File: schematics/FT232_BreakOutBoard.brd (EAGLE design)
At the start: 44.1 x 21.6 mm, 13 parts, among them IC2 FT232RL

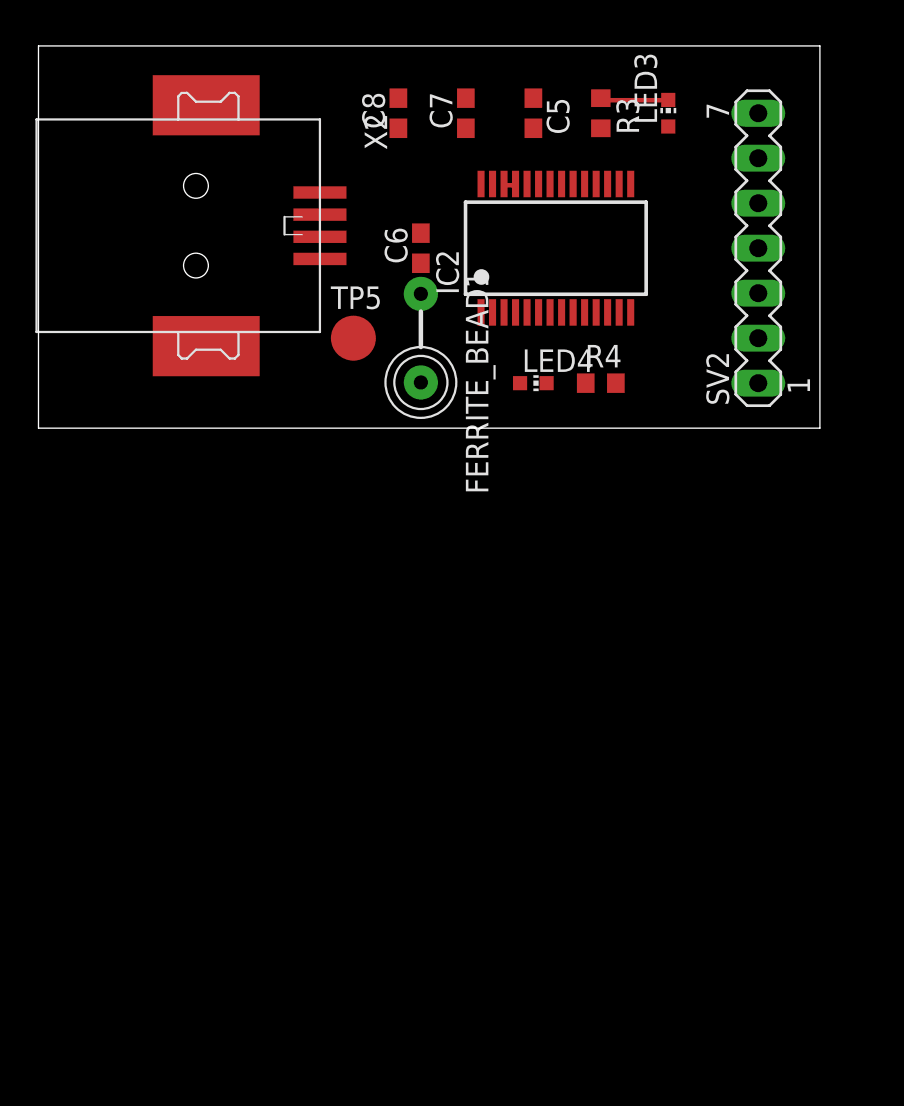
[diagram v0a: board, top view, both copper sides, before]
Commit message: updated breakout board layout and schematic
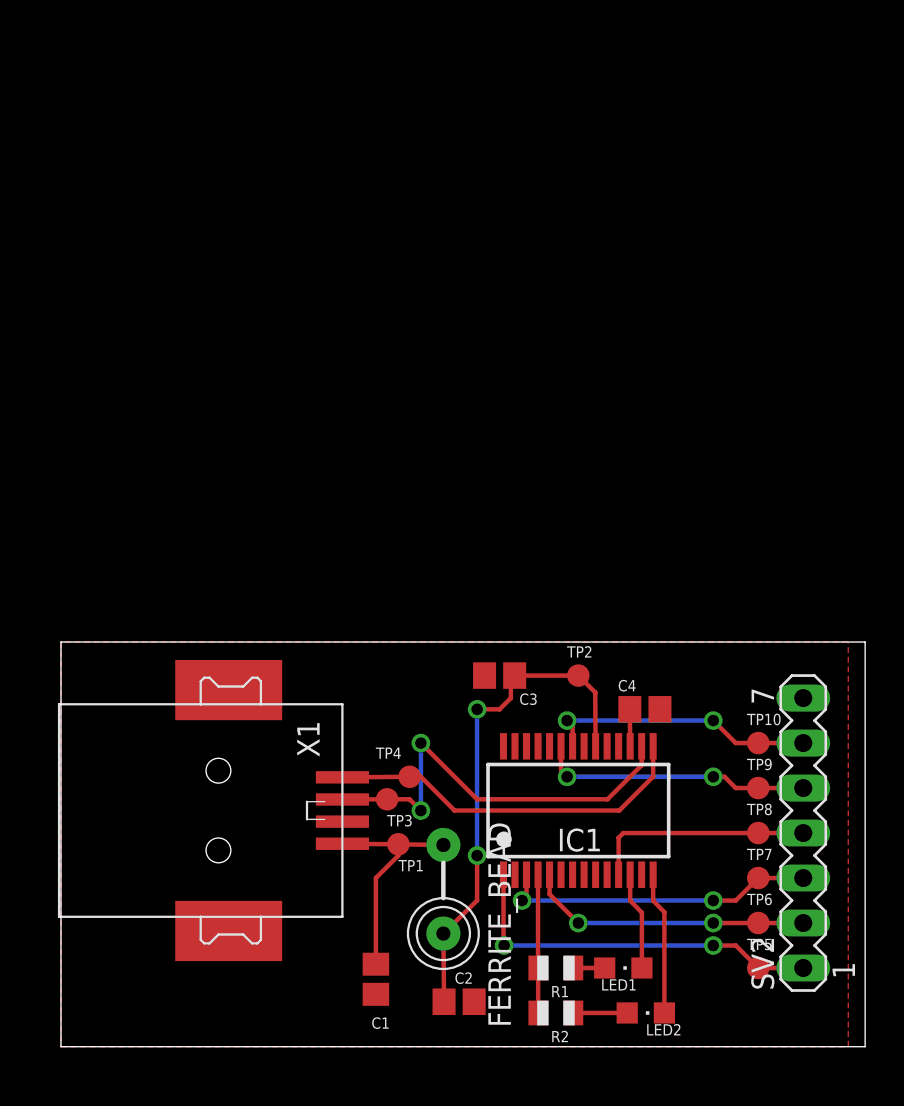
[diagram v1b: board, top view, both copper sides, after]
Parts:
- removed C5, C7: 0.1uF, adafruit:C0603
- removed C6: 10nF, adafruit:C0603
- removed C8: 10uF, adafruit:C0603
- removed FERRITE_BEAD1: FB, adafruit:FB
- removed IC2: FT232RL, ftdichip:SSOP28
- removed LED3, LED4: (no value), adafruit:CHIP-LED0603
- removed R3, R4: 1k, adafruit:R0603
- removed X2: (no value), con-usb-3:USB-B-SMT
- added C1: 10nF, adafruit:C0805
- added C2, C4: 100nF, adafruit:C0805
- added C3: 4.7uF, adafruit:C0805
- added FERRITE_BEAD: FB, adafruit:FB
- added IC1: FT232RL, ftdichip:SSOP28
- added LED1, LED2: (no value), adafruit:CHIPLED_0805
- added R1, R2: (no value), adafruit:R0805
- added TP1, TP10, TP2, TP3, TP4, TP6, TP7, TP8, TP9: TPB1,27, testpad:B1,27
- added X1: USB-B-S, con-usb:USB-B-SMT
- TP5: value TPB2,54 -> TPB1,27; device testpad:B2,54 -> testpad:B1,27
- moved TP5 42.3 mm to (40.6, -19.1)
- moved SV2 33.1 mm to (43.2, -11.4)
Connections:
- removed net N$19: IC2.22, R3.2
- removed net N$20: LED3.C, R3.1
- removed net N$21: C7.1, C8.1, FERRITE_BEAD1.P$2, IC2.20, IC2.4, LED3.A, LED4.A
- removed net N$22: C5.1, IC2.17
- removed net N$23: IC2.15, X2.D+
- removed net N$24: IC2.16, X2.D-
- removed net N$25: IC2.13, R4.2
- removed net N$26: IC2.1, SV2.1
- removed net N$27: LED4.C, R4.1
- removed net N$28: IC2.5, SV2.3
- removed net N$29: IC2.3, SV2.2
- removed net N$31: IC2.23, SV2.7
- removed net N$36: C6.1, FERRITE_BEAD1.P$1, TP5.TP, X2.VUSB
- new net DELEETE: IC1.4, R1.2, R2.2
- new net N$10: IC1.11, SV2.4, TP8.TP
- new net N$11: IC1.23, SV2.5, TP9.TP
- new net N$12: LED2.A, R2.1
- new net N$13: LED1.A, R1.1
- new net N$14: IC1.22, SV2.6, TP10.TP
- new net N$15: IC1.12, LED1.C
- new net N$16: IC1.14, LED2.C
- new net N$17: C2.1, C3.1, FERRITE_BEAD.P$2, IC1.20, TP2.TP
- new net N$6: IC1.1, SV2.1, TP5.TP
- new net N$7: C1.1, FERRITE_BEAD.P$1, TP1.TP, X1.VUSB
- new net N$8: IC1.5, SV2.2, TP6.TP
- new net N$9: IC1.3, SV2.3, TP7.TP
- net GND: now also C1.2, C2.2, C3.2, C4.2, IC1.18, IC1.21, IC1.25, IC1.7; no longer C5.2, C6.2, C7.2, C8.2, IC2.18, IC2.21, IC2.25, IC2.26, IC2.7, X2.GND
- net N$2: now also C4.1, IC1.17; no longer IC2.12, SV2.4
- net N$3: now also IC1.15, TP4.TP, X1.D+; no longer IC2.19, SV2.6
- net N$5: now also IC1.16, TP3.TP, X1.D-; no longer IC2.11, SV2.5
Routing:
- net N$17: track 0.00 -> 28.8 mm, vias 0 -> 2
- net N$5: track 0.00 -> 24.1 mm, vias 0 -> 2
- net N$6: track 0.00 -> 21.4 mm, vias 0 -> 2
- net N$3: track 0.00 -> 20.8 mm
- net N$9: track 0.00 -> 18.0 mm, vias 0 -> 2
- net N$8: track 0.00 -> 16.1 mm, vias 0 -> 2
- net N$11: track 0.00 -> 15.5 mm, vias 0 -> 2
- net N$14: track 0.00 -> 15.4 mm, vias 0 -> 2
- net N$7: track 0.00 -> 14.3 mm
- net N$10: track 0.00 -> 12.6 mm
- net N$16: track 0.00 -> 8.07 mm
- net DELEETE: track 0.00 -> 7.81 mm
- net N$15: track 0.00 -> 5.54 mm
- net N$20: track 3.90 -> 0.00 mm
- net N$12: track 0.00 -> 3.03 mm
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- added copper zone on layer 1, net GND
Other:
- board size 44.1 x 21.6 mm -> 45.4 x 22.9 mm

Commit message: Updated FT232 break-out board with corrected USB connector and larger vias
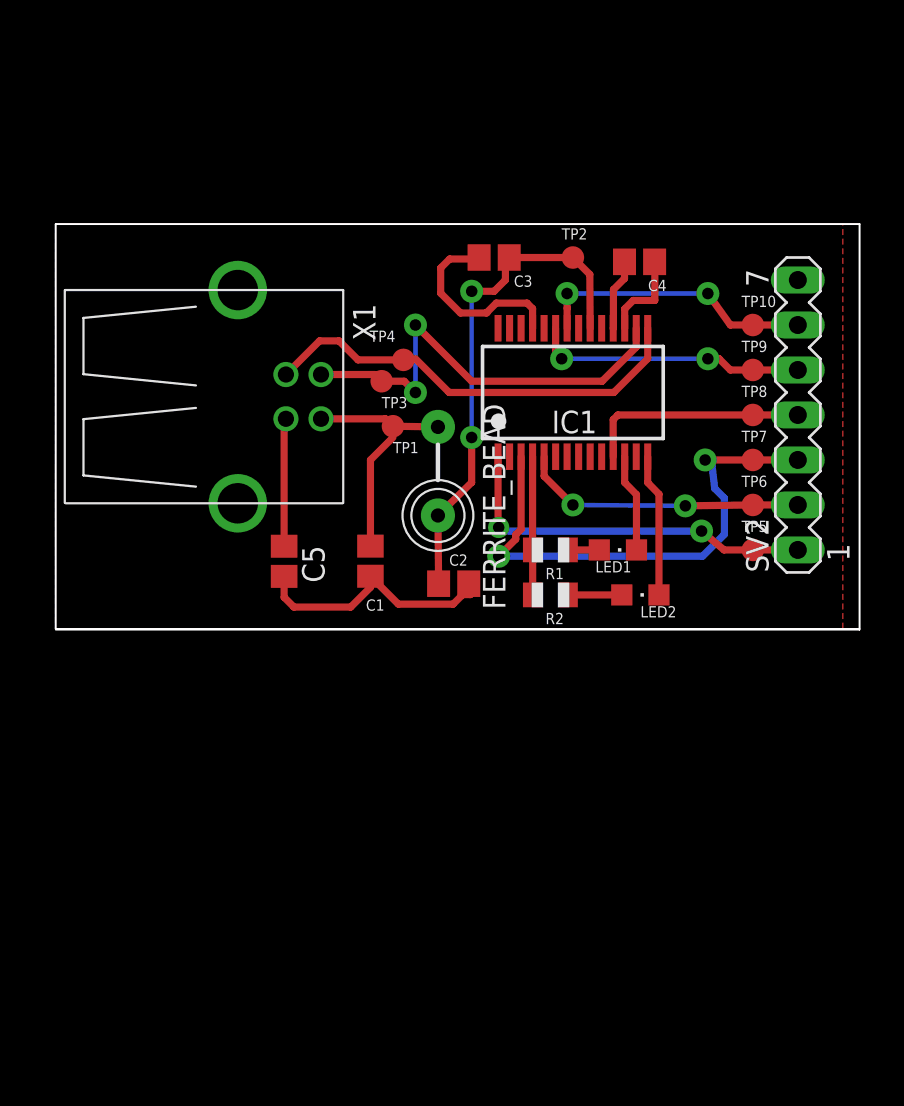
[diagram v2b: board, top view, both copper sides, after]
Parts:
- added C5: 100nF, adafruit:C0805
- X1: value USB-B-S -> USB-B-H; device con-usb:USB-B-SMT -> con-usb:USB-B-H
- moved C4 25.3 mm to (33.9, 20.8), turned to 180 degrees
- moved X1 23.7 mm to (14.0, 13.2)
- moved FERRITE_BEAD 23.6 mm to (22.6, 9.00)
- moved IC1 23.6 mm to (30.2, 13.4)
- moved LED1 23.6 mm to (32.7, 4.55)
- moved LED2 23.6 mm to (34.0, 2.01)
- moved R1 23.6 mm to (28.9, 4.55)
- moved R2 23.6 mm to (28.9, 2.01)
- moved SV2 23.6 mm to (42.9, 12.2)
- moved TP1 23.6 mm to (20.0, 11.5)
- moved TP10 23.6 mm to (40.3, 17.3)
- moved TP3 23.6 mm to (19.4, 14.1)
- moved TP5 23.6 mm to (40.3, 4.55)
- moved TP6 23.6 mm to (40.3, 7.09)
- moved TP7 23.6 mm to (40.3, 9.63)
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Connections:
- new net N$1: C5.1, X1.GND
- net GND: now also C5.2
- net N$7: now also X1.VBUS; no longer X1.VUSB
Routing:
- net GND: track 0.00 -> 29.5 mm
- net N$9: track 18.0 -> 29.3 mm
- net N$1: track 0.00 -> 7.24 mm
- net N$3: track 20.8 -> 25.0 mm
- net N$2: track 2.09 -> 5.17 mm
- net N$5: track 24.1 -> 25.2 mm
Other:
- outline, holes or cut-outs redrawn
